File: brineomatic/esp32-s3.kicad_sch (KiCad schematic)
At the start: 47 parts, among them J23 USB_TYPE_C_16PIN, Q7 FDC6330L, Q8 S8050, Q9 S8050, SW1 RESET, SW2 BOOT, U10 CH343P, U6 ESP32-S3-WROOM-1-N16R8, U7 USBLC6-2SC6, U8 XC6210B332MR, U9 CH334F, Y1 12Mhz, Y2 32.768kHz

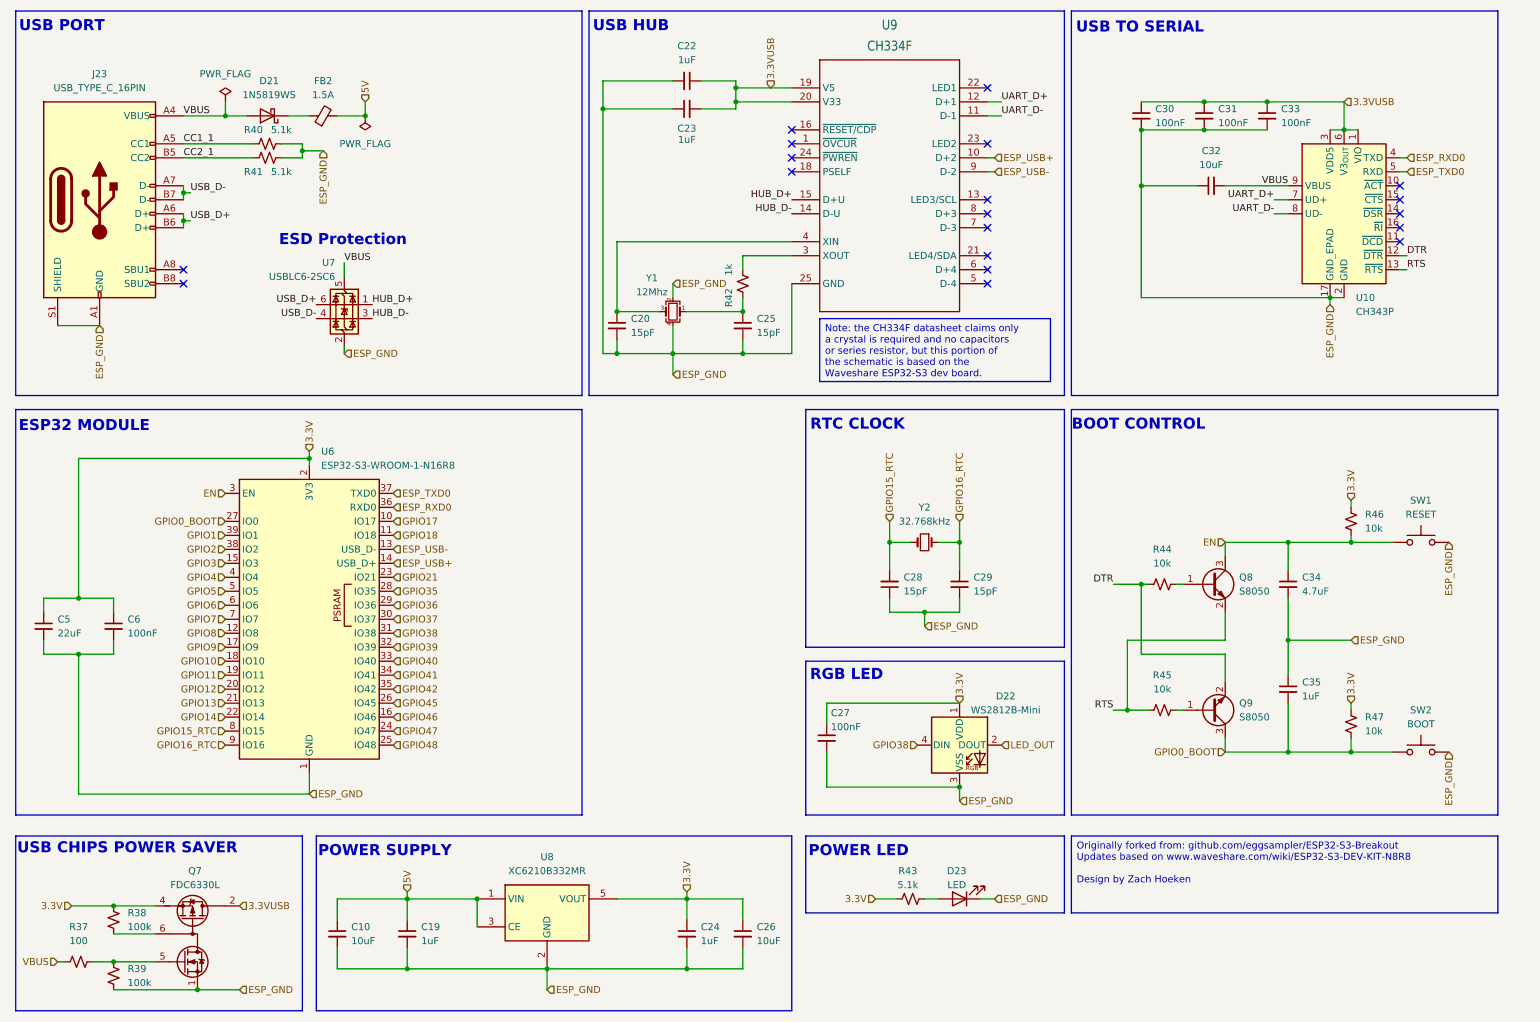
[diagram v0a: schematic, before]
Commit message: tmc2209 driver schematic checked and laid out nicely.
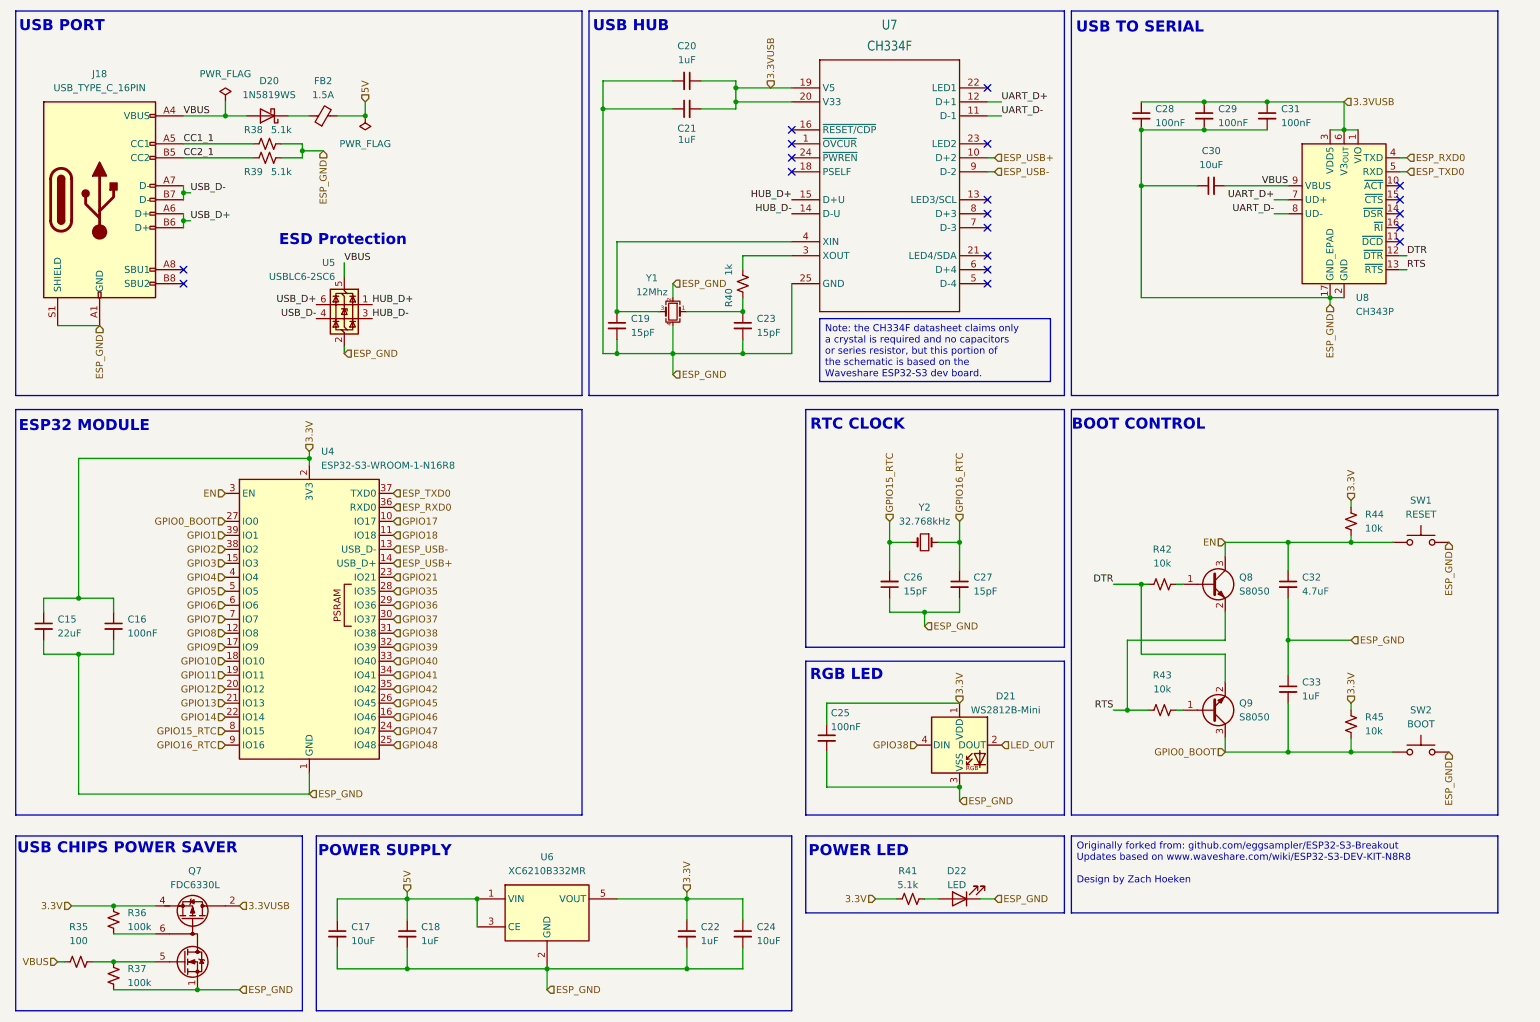
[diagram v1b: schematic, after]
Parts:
- renumbered C5 to C15, C6 to C16, C10 to C17, C19 to C18, C20 to C19, C22 to C20, C23 to C21, C24 to C22, C25 to C23, C26 to C24, C27 to C25, C28 to C26, C29 to C27, C30 to C28, C31 to C29, C32 to C30, C33 to C31, C34 to C32, C35 to C33, D21 to D20, D22 to D21, D23 to D22, J23 to J18, R37 to R35, R38 to R36, R39 to R37, R40 to R38, R41 to R39, R42 to R40, R43 to R41, R44 to R42, R45 to R43, R46 to R44, R47 to R45, U6 to U4, U7 to U5, U8 to U6, U9 to U7, U10 to U8

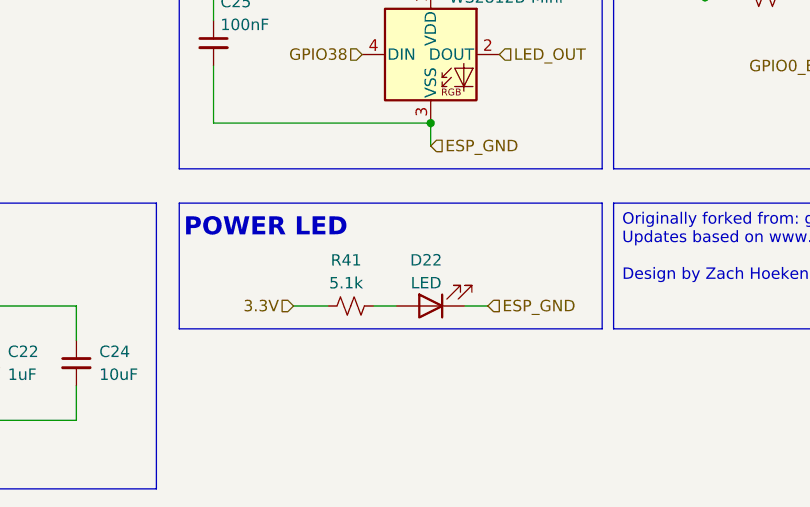
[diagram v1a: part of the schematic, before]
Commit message: single 5v supply works just fine
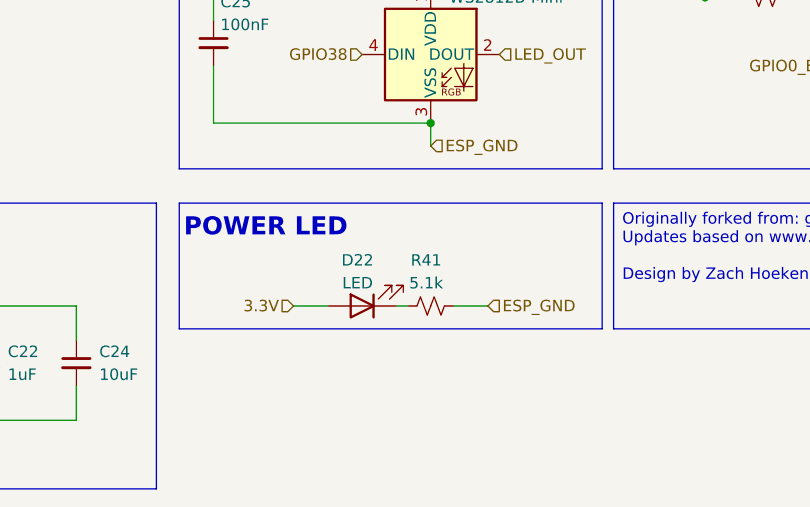
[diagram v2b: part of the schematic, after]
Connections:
- net 3.3V: now also D22.2 (A); no longer R41.1
- net ESP_GND: now also R41.2; no longer D22.1 (K)
- new net: D22.1 (K), R41.1
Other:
- moved on the sheet: D22, R41
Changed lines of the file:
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@@
-	(wire
-		(pts
-			(xy 189.23 175.26) (xy 191.77 175.26)
-		)
-		(stroke
-			(width 0)
-			(type default)
-		)
-	)
 	(wire
 		(pts
@@
 	(wire
 		(pts
+			(xy 181.61 175.26) (xy 182.88 175.26)
+		)
+		(stroke
+			(width 0)
+			(type default)
+		)
+	)
+	(wire
+		(pts
 			(xy 233.68 110.49) (xy 245.11 110.49)
 		)
@@
 	(wire
 		(pts
-			(xy 179.07 175.26) (xy 181.61 175.26)
-		)
-		(stroke
-			(width 0)
-			(type default)
-		)
-	)
-	(wire
-		(pts
 			(xy 256.54 102.87) (xy 256.54 104.14)
 		)
@@
 		(pts
 			(xy 72.39 187.96) (xy 72.39 184.15)
+		)
+		(stroke
+			(width 0)
+			(type default)
+		)
+	)
+	(wire
+		(pts
+			(xy 187.96 175.26) (xy 191.77 175.26)
 		)
 		(stroke
@@
 	(symbol
 		(lib_id "Device:LED")
-		(at 185.42 175.26 180)
+		(at 177.8 175.26 180)
 		(unit 1)
 		(exclude_from_sim no)
@@
 		(dnp no)
 		(property "Reference" "D22"
-			(at 184.912 170.18 0)
+			(at 177.292 170.18 0)
 			(effects
 				(font
@@
 		)
 		(property "Value" "LED"
-			(at 184.912 172.72 0)
+			(at 177.292 172.72 0)
 			(effects
 				(font
@@
 		)
 		(property "Footprint" "LED_SMD:LED_0603_1608Metric"
-			(at 185.42 175.26 0)
+			(at 177.8 175.26 0)
 			(effects
 				(font
@@
 		)
 		(property "Datasheet" "~"
-			(at 185.42 175.26 0)
+			(at 177.8 175.26 0)
 			(effects
 				(font
@@
 		)
 		(property "Description" "Light emitting diode"
-			(at 185.42 175.26 0)
+			(at 177.8 175.26 0)
 			(effects
 				(font
@@
 		)
 		(property "Sim.Pins" "1=K 2=A"
-			(at 185.42 175.26 0)
+			(at 177.8 175.26 0)
 			(effects
 				(font
@@
 		)
 		(property "LCSC" "C2286"
-			(at 185.42 175.26 0)
+			(at 177.8 175.26 0)
 			(effects
 				(font
@@
 	(symbol
 		(lib_id "Device:R_Small_US")
-		(at 176.53 175.26 90)
+		(at 185.42 175.26 90)
 		(unit 1)
 		(exclude_from_sim no)
@@
 		(dnp no)
 		(property "Reference" "R41"
-			(at 176.022 170.18 90)
+			(at 184.912 170.18 90)
 			(effects
 				(font
@@
 		)
 		(property "Value" "5.1k"
-			(at 176.022 172.72 90)
+			(at 184.912 172.72 90)
 			(effects
 				(font
@@
 		)
 		(property "Footprint" "Resistor_SMD:R_0603_1608Metric"
-			(at 176.53 175.26 0)
+			(at 185.42 175.26 0)
 			(effects
 				(font
@@
 		)
 		(property "Datasheet" "~"
-			(at 176.53 175.26 0)
+			(at 185.42 175.26 0)
 			(effects
 				(font
@@
 		)
 		(property "Description" "Resistor, small US symbol"
-			(at 176.53 175.26 0)
-			(effects
-				(font
+			(at 185.42 175.26 0)
+			(effects
+				(font

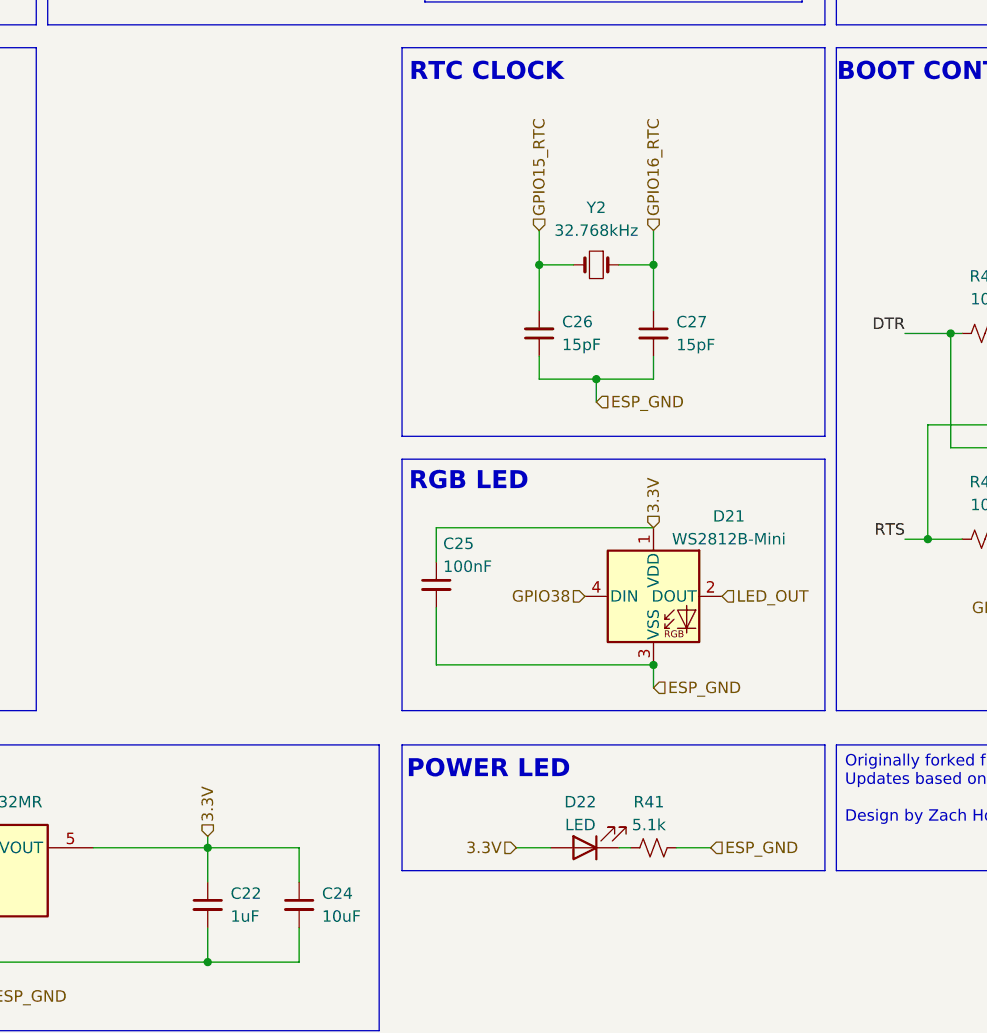
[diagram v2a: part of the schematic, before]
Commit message: aligned all connectors with board edge
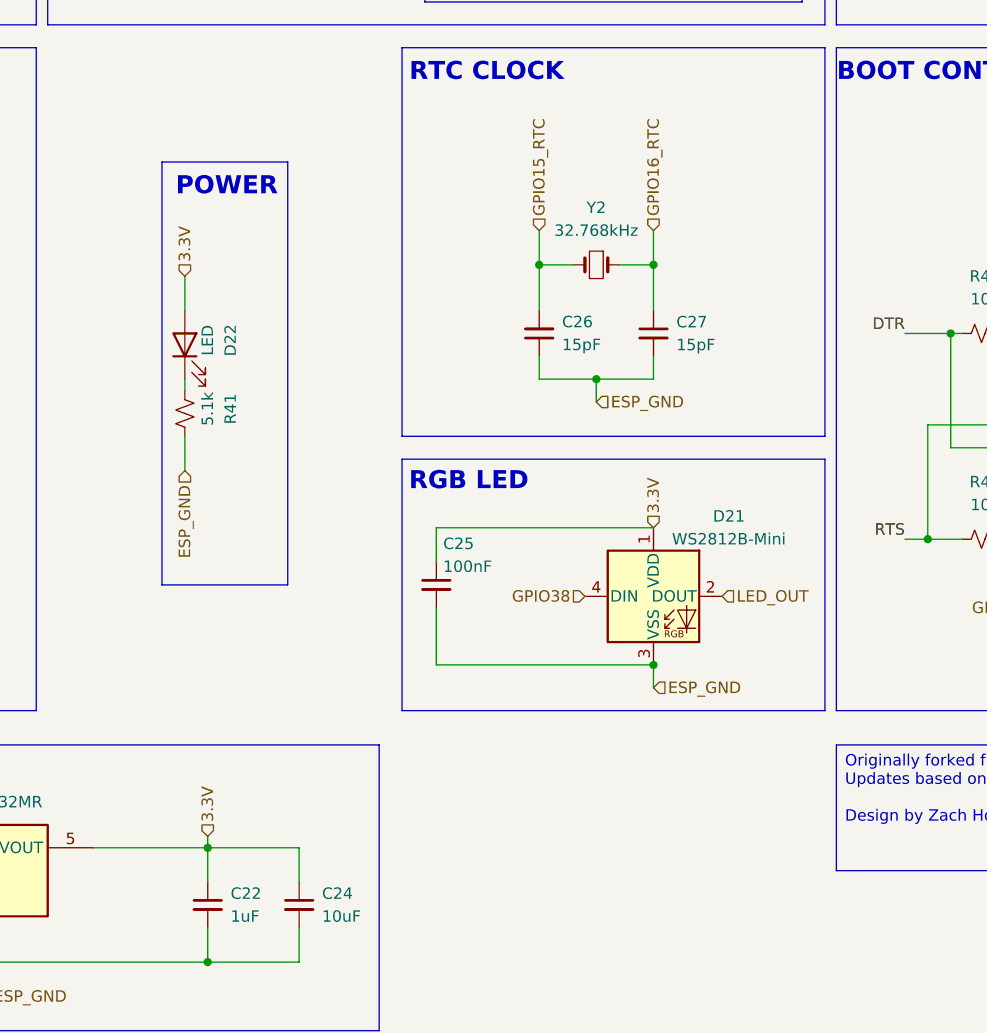
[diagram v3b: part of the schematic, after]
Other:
- note added: "POWER"
- note removed: "POWER LED"
- moved on the sheet: D22, R41
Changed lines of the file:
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@@
 	)
 	(rectangle
-		(start 157.48 163.83)
-		(end 204.47 177.8)
+		(start 144.78 99.06)
+		(end 130.81 146.05)
 		(stroke
 			(width 0)
@@
 		)
 	)
-	(text "POWER LED"
+	(text "POWER"
 		(exclude_from_sim no)
-		(at 157.988 166.624 0)
+		(at 132.334 101.854 0)
 		(effects
 			(font
@@
 	(wire
 		(pts
-			(xy 170.18 175.26) (xy 173.99 175.26)
+			(xy 133.35 111.76) (xy 133.35 115.57)
 		)
 		(stroke
@@
 	(wire
 		(pts
-			(xy 181.61 175.26) (xy 182.88 175.26)
+			(xy 133.35 123.19) (xy 133.35 124.46)
 		)
 		(stroke
@@
 	(wire
 		(pts
-			(xy 187.96 175.26) (xy 191.77 175.26)
+			(xy 133.35 129.54) (xy 133.35 133.35)
 		)
 		(stroke
@@
 	(hierarchical_label "ESP_GND"
 		(shape input)
-		(at 191.77 175.26 0)
+		(at 133.35 133.35 270)
 		(effects
 			(font
 				(size 1.27 1.27)
 			)
-			(justify left)
+			(justify right)
 		)
 	)
@@
 	(hierarchical_label "3.3V"
 		(shape input)
-		(at 170.18 175.26 180)
+		(at 133.35 111.76 90)
 		(effects
 			(font
 				(size 1.27 1.27)
 			)
-			(justify right)
+			(justify left)
 		)
 	)
@@
 	(symbol
 		(lib_id "Device:LED")
-		(at 177.8 175.26 180)
+		(at 133.35 119.38 90)
 		(unit 1)
 		(exclude_from_sim no)
@@
 		(dnp no)
 		(property "Reference" "D22"
-			(at 177.292 170.18 0)
+			(at 138.43 118.872 0)
 			(effects
 				(font
@@
 		)
 		(property "Value" "LED"
-			(at 177.292 172.72 0)
+			(at 135.89 118.872 0)
 			(effects
 				(font
@@
 		)
 		(property "Footprint" "LED_SMD:LED_0603_1608Metric"
-			(at 177.8 175.26 0)
+			(at 133.35 119.38 0)
 			(effects
 				(font
@@
 		)
 		(property "Datasheet" "~"
-			(at 177.8 175.26 0)
+			(at 133.35 119.38 0)
 			(effects
 				(font
@@
 		)
 		(property "Description" "Light emitting diode"
-			(at 177.8 175.26 0)
+			(at 133.35 119.38 0)
 			(effects
 				(font
@@
 		)
 		(property "Sim.Pins" "1=K 2=A"
-			(at 177.8 175.26 0)
+			(at 133.35 119.38 0)
 			(effects
 				(font
@@
 		)
 		(property "LCSC" "C2286"
-			(at 177.8 175.26 0)
+			(at 133.35 119.38 0)
 			(effects
 				(font
@@
 	(symbol
 		(lib_id "Device:R_Small_US")
-		(at 185.42 175.26 90)
+		(at 133.35 127 0)
 		(unit 1)
 		(exclude_from_sim no)
@@
 		(dnp no)
 		(property "Reference" "R41"
-			(at 184.912 170.18 90)
+			(at 138.43 126.492 90)
 			(effects
 				(font
@@
 		)
 		(property "Value" "5.1k"
-			(at 184.912 172.72 90)
+			(at 135.89 126.492 90)
 			(effects
 				(font
@@
 		)
 		(property "Footprint" "Resistor_SMD:R_0603_1608Metric"
-			(at 185.42 175.26 0)
+			(at 133.35 127 0)
 			(effects
 				(font
@@
 		)
 		(property "Datasheet" "~"
-			(at 185.42 175.26 0)
+			(at 133.35 127 0)
 			(effects
 				(font
@@
 		)
 		(property "Description" "Resistor, small US symbol"
-			(at 185.42 175.26 0)
+			(at 133.35 127 0)
 			(effects
 				(font
